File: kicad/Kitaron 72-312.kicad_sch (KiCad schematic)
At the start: 35 parts, among them J1 Audio Jack, Q1 2SB33, Q2 2N1305, Q3 2SB33, Q4 2SB263, Q5 2SB263, SW2 RotaryEncoder_Switch, T1 Transformer, T2 Transformer

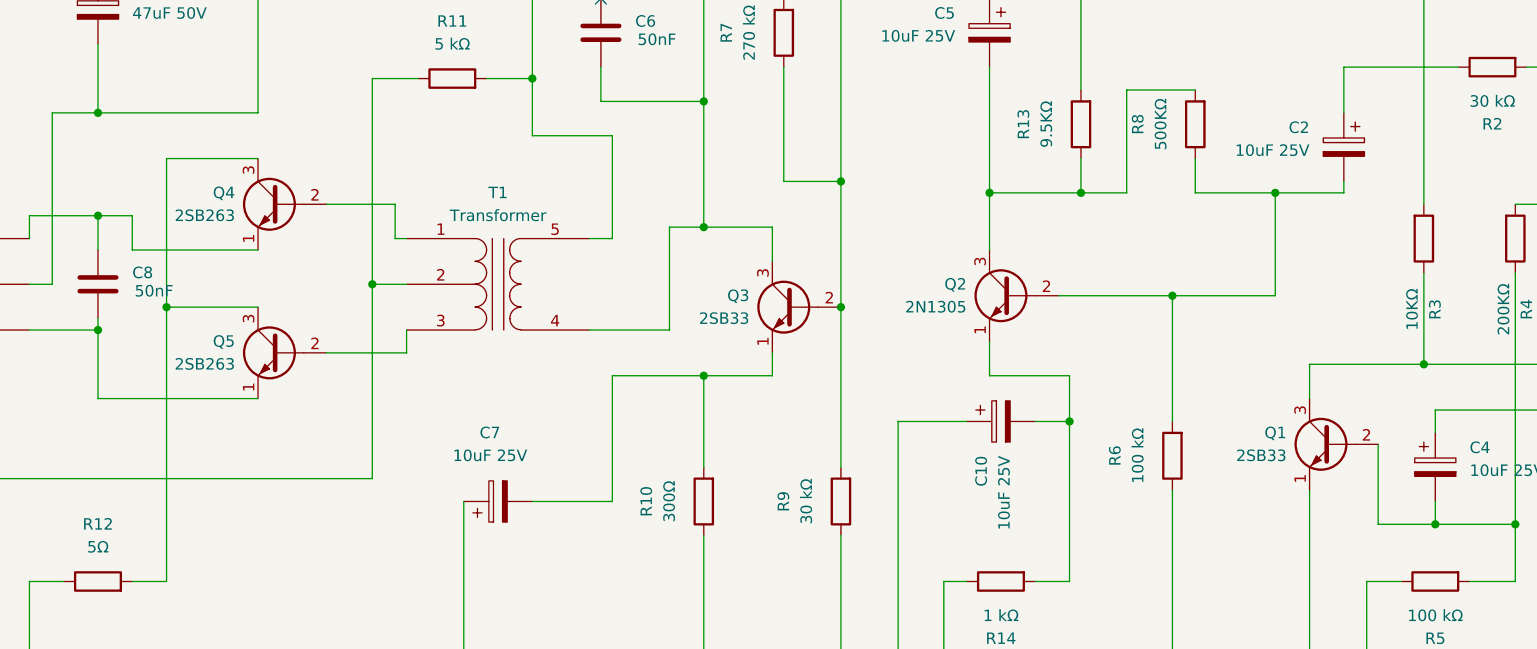
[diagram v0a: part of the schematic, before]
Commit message: Fixed transistor type - from NPN to PNP
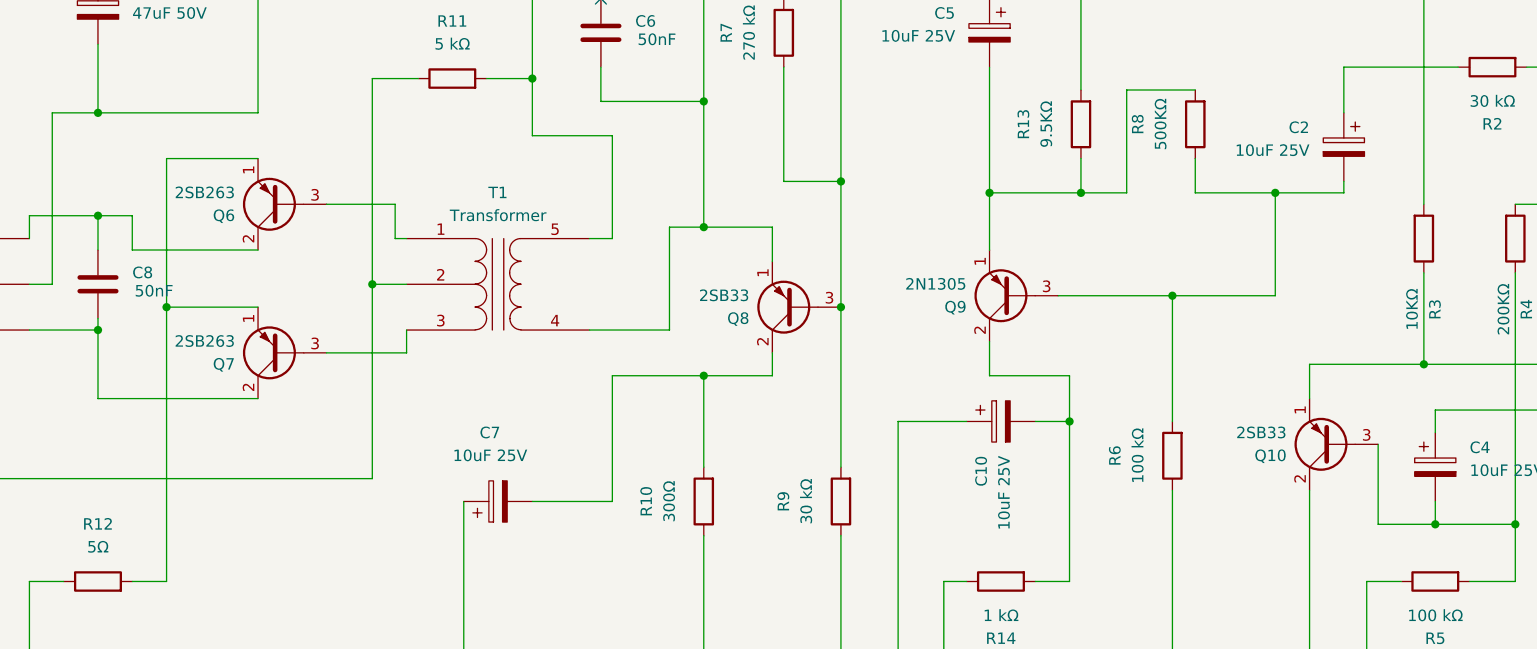
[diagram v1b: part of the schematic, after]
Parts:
- removed Q1, Q3: 2SB33, Package_TO_SOT_THT:TO-18-3, symbol Transistor_BJT:BC107
- removed Q2: 2N1305, Package_TO_SOT_THT:TO-18-3, symbol Transistor_BJT:BC107
- removed Q4, Q5: 2SB263, Package_TO_SOT_THT:TO-18-3, symbol Transistor_BJT:BC107
- added Q10, Q8: 2SB33, Package_TO_SOT_THT:TO-126-3_Vertical, symbol Transistor_BJT:2SB631
- added Q6, Q7: 2SB263, Package_TO_SOT_THT:TO-126-3_Vertical, symbol Transistor_BJT:2SB631
- added Q9: 2N1305, Package_TO_SOT_THT:TO-126-3_Vertical, symbol Transistor_BJT:2SB631
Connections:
- net GND: now also Q10.2 (C)
- net at C8.1, T2.1 (PR1): now also Q6.2 (C)
- net at C8.2, T2.3 (PR2): now also Q7.2 (C)
- net at C4.2, R4.1, R5.2: now also Q10.3 (B)
- net at C3.2, R3.1, R4.2: now also Q10.1 (E)
- net at C10.2, R14.2: now also Q9.2 (C)
- net at C2.2, R6.2, R8.1: now also Q9.3 (B)
- net at C5.2, R13.1, R8.2: now also Q9.1 (E)
- net at R12.2: now also Q6.1 (E), Q7.1 (E)
- net at T1.3 (PR2): now also Q7.3 (B)
- net at C6.2, R7.2, T1.4 (S1): now also Q8.1 (E)
- net at T1.1 (PR1): now also Q6.3 (B)
- net at C5.1, R7.1, R9.2: now also Q8.3 (B)
- net at C7.2, R10.2: now also Q8.2 (C)
